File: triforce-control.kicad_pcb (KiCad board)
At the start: 2 copper layers, 107.9 x 64.8 mm, 25 parts, among them U1 ADAFRUIT_HUZZAH, U2 bno055, U3 LPC1768

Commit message: Started new PCB design.
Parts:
- removed CON_D1: Drive Motor 1, mbed:AngledServoCon
- removed CON_D2: Drive Motor 2, mbed:AngledServoCon
- removed CON_D3: Drive Motor 3, mbed:AngledServoCon
- removed CON_RX_D1: Drive Chan 1, mbed:AngledServoCon
- removed CON_RX_D2: Drive Chan 2, mbed:AngledServoCon
- removed CON_RX_D3: Drive Chan 3, mbed:AngledServoCon
- removed CON_RX_D4: Drive Chan 4, mbed:AngledServoCon
- removed CON_RX_D5: Drive Chan 5, mbed:AngledServoCon
- removed CON_RX_D6: Drive Chan 6, mbed:AngledServoCon
- removed CON_RX_W1: Weapon Chan 1, mbed:AngledServoCon
- removed CON_RX_W2: Weapon Chan 2, mbed:AngledServoCon
- removed CON_RX_W3: Weapon Chan 3, mbed:AngledServoCon
- removed CON_RX_W4: Weapon Chan 4, mbed:AngledServoCon
- removed CON_RX_W5: Weapon Chan 5, mbed:AngledServoCon
- removed CON_RX_W6: Weapon Chan 6, mbed:AngledServoCon
- removed CON_W1, CON_W2, CON_W3: Weapon Motor 1, mbed:AngledServoCon
- removed REF** (x4): MountingHole_3.2mm_M3_ISO7380, Mounting_Holes:MountingHole_3.2mm_M3_ISO7380
- added CON1: Conn_01x08, Connectors_JST:JST_PH_S8B-PH-K_08x2.00mm_Angled, B.Cu at (105.4, 69.8)
- added CON2: Conn_01x08, Connectors_JST:JST_PH_S8B-PH-K_08x2.00mm_Angled, B.Cu at (141.6, 69.8)
- added CON3: CON_ESC_W1, mbed:Pin_Header_Angled_3x01_Pitch2.54mm, F.Cu at (135.3, 127.0)
- added CON4: CON_ESC_W2, mbed:Pin_Header_Angled_3x01_Pitch2.54mm, F.Cu at (137.8, 127.0)
- added CON5: CON_ESC_W3, mbed:Pin_Header_Angled_3x01_Pitch2.54mm, F.Cu at (140.3, 127.0)
- added CON6: CON_ESC_D1, mbed:Pin_Header_Angled_3x01_Pitch2.54mm, F.Cu at (142.9, 127.0)
- added CON7: CON_ESC_D2, mbed:Pin_Header_Angled_3x01_Pitch2.54mm, F.Cu at (145.4, 127.0)
- added CON8: CON_ESC_D3, mbed:Pin_Header_Angled_3x01_Pitch2.54mm, F.Cu at (148.0, 127.0)
- added CON9: Conn_01x04, Connectors_JST:JST_PH_S4B-PH-K_04x2.00mm_Angled, F.Cu at (154.7, 126.4)
- added U4: SN65HVD232, Housings_SOIC:SOIC-8_3.9x4.9mm_Pitch1.27mm, B.Cu at (158.1, 139.2)
- moved U3 31.9 mm to (127.0, 94.0), turned to 180 degrees
- moved U1 31.4 mm to (143.5, 86.4)
- moved U2 29.3 mm to (104.1, 137.2), turned to 90 degrees
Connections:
- U3 pad 11: IN_RX_W5 -> IN_RX_W2
- U3 pad 12: IN_RX_W6 -> IN_RX_W1
- U3 pad 19: Net-(U3-Pad19) -> ESP_READY
- U3 pad 21: PWM_OUT_DRV_MOTOR_1 -> PWM_OUT_DRV_MOTOR_3
- U3 pad 23: PWM_OUT_DRV_MOTOR_3 -> PWM_OUT_DRV_MOTOR_1
- U3 pad 24: PWM_OUT_WPN_MOTOR_1 -> PWM_OUT_WPN_MOTOR_3
- U3 pad 26: PWM_OUT_WPN_MOTOR_3 -> PWM_OUT_WPN_MOTOR_1
- U3 pad 29: ESP_READY -> CAN_TXD
- U3 pad 30: Net-(U3-Pad30) -> CAN_RXD
- U3 pad 40: Net-(U3-Pad40) -> MBED_3V3
- U3 pad 5: IN_RX_W1 -> IN_RX_W6
- U3 pad 6: IN_RX_W2 -> IN_RX_W5
- U3 pad 7: IN_RX_W3 -> IN_RX_W4
- U3 pad 8: IN_RX_W4 -> IN_RX_W3
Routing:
- net CAN_TXD: track 0.00 -> 93.9 mm
- net CAN_RXD: track 0.00 -> 85.1 mm
- net MBED_3V3: track 0.00 -> 62.0 mm, vias 0 -> 1
- net IN_RX_W4: track 19.2 -> 72.6 mm
- net IN_RX_W3: track 15.6 -> 68.5 mm
- net IN_RX_W6: track 30.8 -> 80.6 mm
- net IN_RX_W5: track 27.2 -> 76.6 mm
- net IN_RX_W2: track 12.0 -> 59.4 mm
- net IN_RX_W1: track 8.45 -> 55.7 mm
- net +5V: track 194.6 -> 231.5 mm
- net BNO_MBED_SCL: track 56.4 -> 22.4 mm
- net GND: track 213.0 -> 188.2 mm, vias 0 -> 4
- net IN_RX_D6: track 53.9 -> 33.8 mm
- net IN_RX_D1: track 35.9 -> 50.7 mm
- net IN_RX_D5: track 50.3 -> 37.2 mm
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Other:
- board size 107.9 x 64.8 mm -> 74 x 86 mm
- board text added: "Triforce Fight Controller V1"
- board text removed: "DRIVE_RX"
- board text removed: "ESC OUT"
- board text removed: "WEAPON_RX"

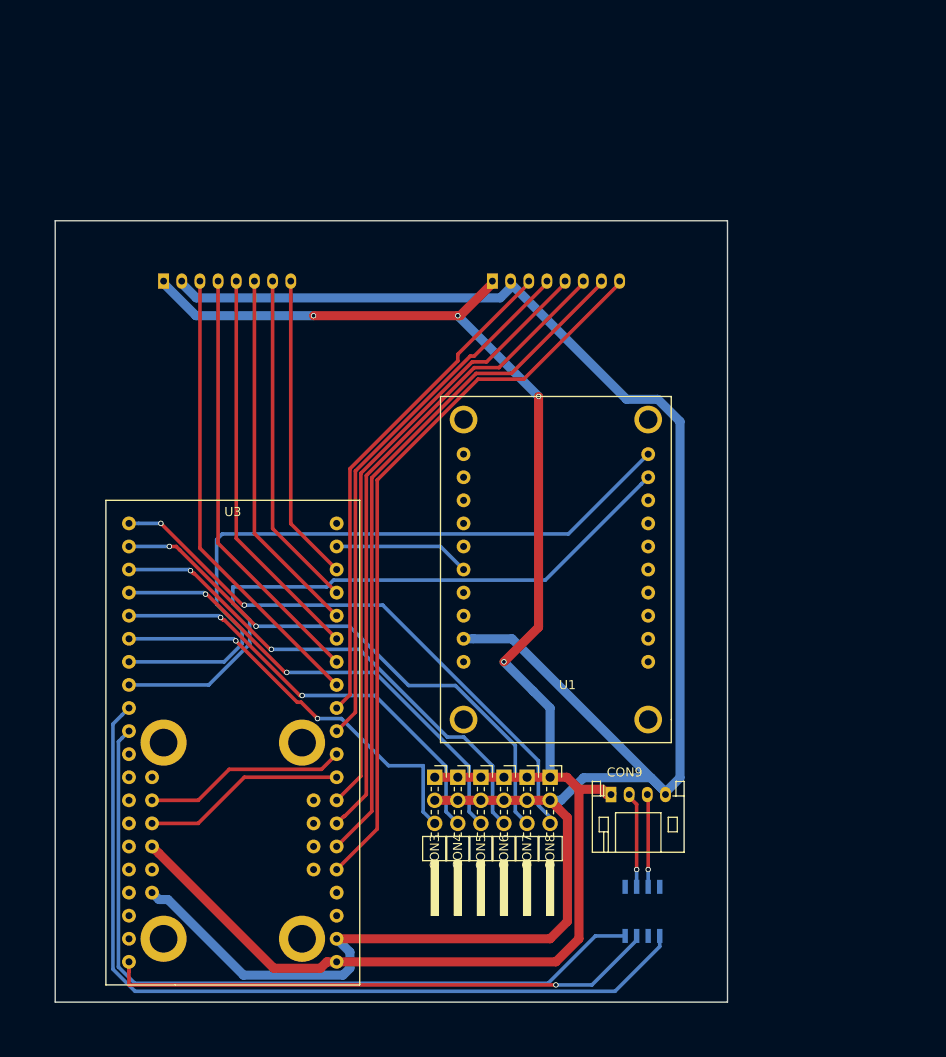
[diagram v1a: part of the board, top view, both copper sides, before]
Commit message: Added missing GND connection.
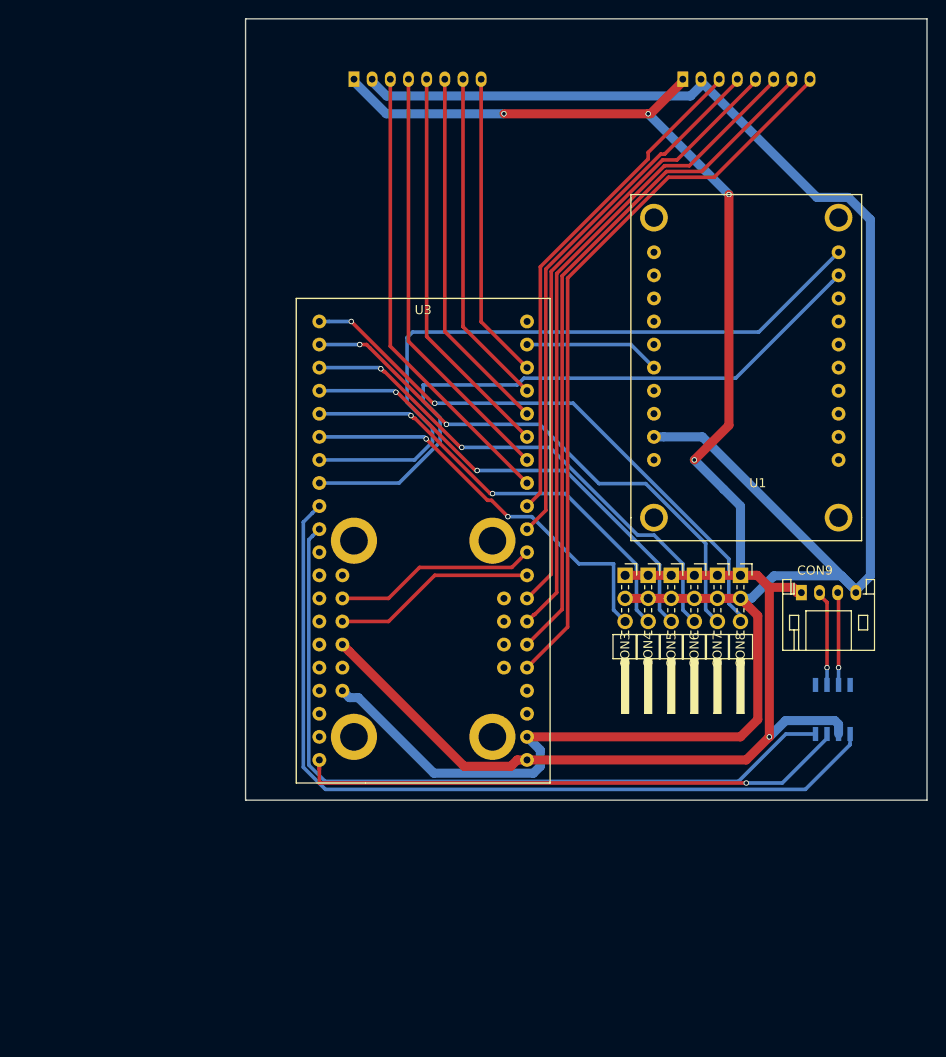
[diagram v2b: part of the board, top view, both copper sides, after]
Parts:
- moved U3 30.5 mm to (148.0, 71.8)
- moved CON2 30.5 mm to (162.6, 47.6)
- moved CON3 30.5 mm to (156.2, 104.8)
- moved CON4 30.5 mm to (158.8, 104.8)
- moved CON6 30.5 mm to (163.8, 104.8)
- moved CON7 30.5 mm to (166.4, 104.8)
- moved CON9 30.5 mm to (175.6, 104.1)
- moved U1 30.5 mm to (164.5, 64.1)
- moved CON1 30.5 mm to (126.4, 47.6)
- moved U2 30.5 mm to (125.1, 114.9)
- moved CON5 30.5 mm to (161.3, 104.8)
- moved CON8 30.5 mm to (168.9, 104.8)
- moved U4 30.5 mm to (179.1, 117.0)
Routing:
- net GND: track 188.2 -> 197.8 mm, vias 4 -> 5
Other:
- board size 74 x 86 mm -> 75 x 86 mm

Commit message: Prettifying the front silkscreen with symbols and text.
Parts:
- added G***: LOGO, mbed:logo_small, F.Cu at (134.0, 54.6)
- added REF***: OSHW-Logo2_14.6x12mm_SilkScreen, Symbols:OSHW-Logo2_14.6x12mm_SilkScreen, F.Cu at (134.0, 80.6)
- added REF***: KiCad-Logo2_6mm_SilkScreen, Symbols:KiCad-Logo2_6mm_SilkScreen, F.Cu at (151.8, 45.1)
- added REF1: MountingHole_3.2mm_M3_ISO14580_Pad, Mounting_Holes:MountingHole_3.2mm_M3_ISO14580_Pad, F.Cu at (120.0, 56.0)
- added REF2: MountingHole_3.2mm_M3_ISO14580_Pad, Mounting_Holes:MountingHole_3.2mm_M3_ISO14580_Pad, F.Cu at (184.0, 56.0)
- added REF3: MountingHole_3.2mm_M3_ISO14580_Pad, Mounting_Holes:MountingHole_3.2mm_M3_ISO14580_Pad, F.Cu at (152.0, 114.0)
- added U3: LPC1768, mbed:lpc1768, F.Cu at (148.0, 71.8)
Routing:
- net (no net): track 2.54 -> 0.00 mm
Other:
- board text added: "CAN BUS"
- board text added: "DRIVE RX"
- board text added: "DRV"
- board text added: "ESC PWM OUT"
- board text added: "TeamTriforceUK"
- board text added: "WEAPON RX"
- board text added: "WPN"
- board text added: "fb.com/TeamTriforceUK"
- board text added: "github.com/TeamTriforceUK"
- board text removed: "Triforce Fight Controller"

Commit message: Changed tracks.
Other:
- board text added: "Triforce Fight Controller v1.0 (keffel)"
- board text removed: "Rev. A"
- board text removed: "Triforce Fight Controller V1"

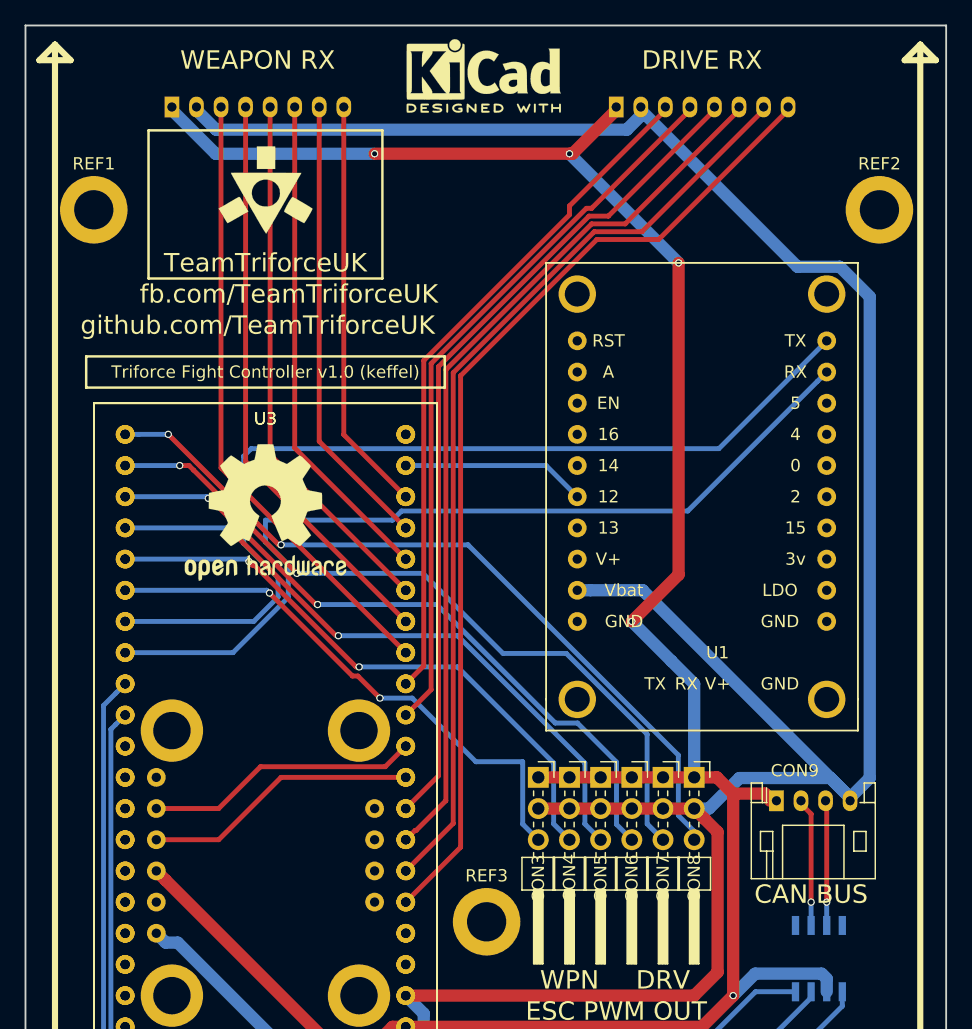
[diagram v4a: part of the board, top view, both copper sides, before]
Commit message: Swapped JSP PH for JST SH on RX inputs.
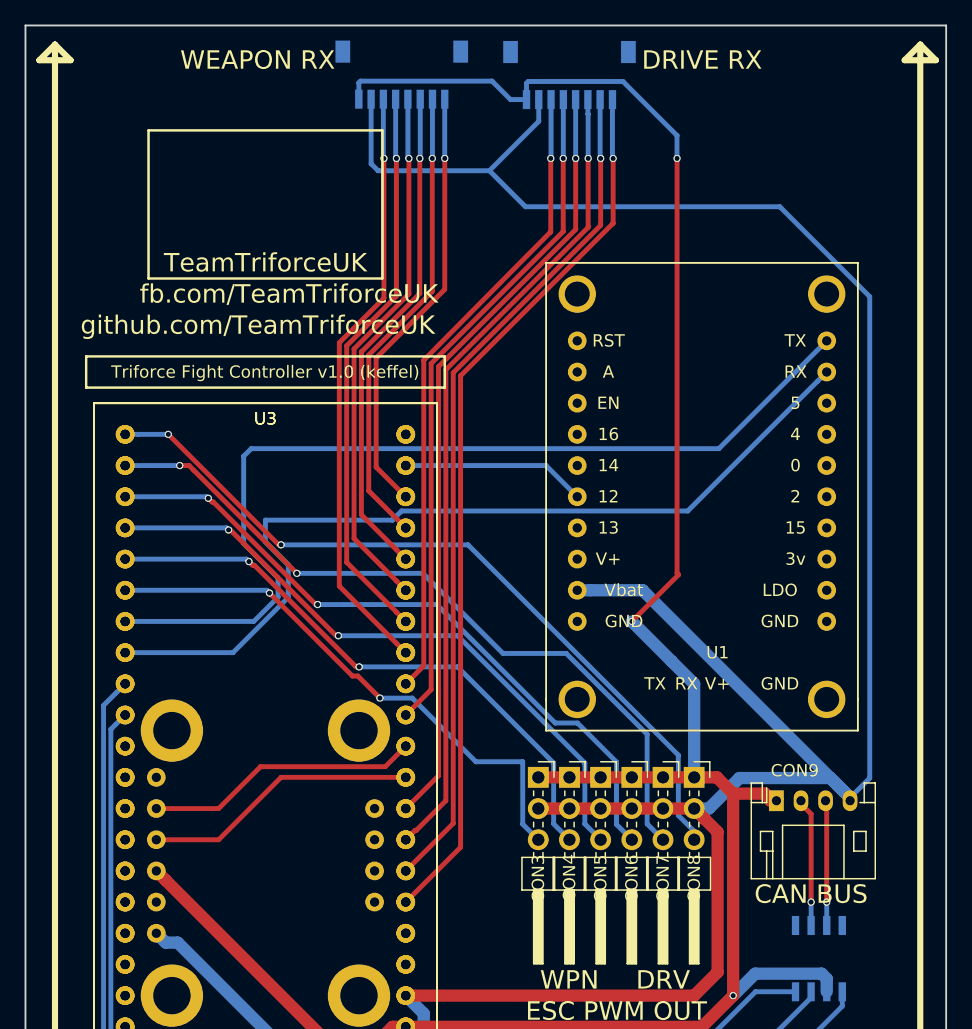
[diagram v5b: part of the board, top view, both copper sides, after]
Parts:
- removed G***: LOGO, mbed:logo_small
- removed REF***: OSHW-Logo2_14.6x12mm_SilkScreen, Symbols:OSHW-Logo2_14.6x12mm_SilkScreen
- removed REF***: KiCad-Logo2_6mm_SilkScreen, Symbols:KiCad-Logo2_6mm_SilkScreen
- removed REF1, REF2, REF3: MountingHole_3.2mm_M3_ISO14580_Pad, Mounting_Holes:MountingHole_3.2mm_M3_ISO14580_Pad
- CON1, CON2: footprint Connectors_JST:JST_PH_S8B-PH-K_08x2.00mm_Angled -> Connectors_JST:JST_SH_SM08B-SRSS-TB_08x1.00mm_Angled
- moved CON1 18.9 mm to (145.1, 45.1)
- moved CON2 4.58 mm to (158.8, 45.1)
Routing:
- net GND: track 197.8 -> 187.1 mm, vias 5 -> 3
- net IN_RX_W6: track 80.6 -> 72.5 mm, vias 0 -> 1
- net IN_RX_W5: track 76.6 -> 69.4 mm, vias 0 -> 1
- net IN_RX_W4: track 72.6 -> 66.5 mm, vias 0 -> 1
- net +5V: track 231.5 -> 225.9 mm
- net IN_RX_W3: track 68.5 -> 63.5 mm, vias 0 -> 1
- net IN_RX_W2: track 59.4 -> 55.4 mm, vias 0 -> 1
- net IN_RX_W1: track 55.7 -> 52.5 mm, vias 0 -> 1
- net IN_RX_D6: track 33.8 -> 35.7 mm, vias 0 -> 1
- net IN_RX_D1: track 50.7 -> 48.9 mm, vias 0 -> 1
- net IN_RX_D5: track 37.2 -> 38.3 mm, vias 0 -> 1
- net IN_RX_D2: track 47.3 -> 46.2 mm, vias 0 -> 1
- net IN_RX_D4: track 40.6 -> 40.9 mm, vias 0 -> 1
- net IN_RX_D3: track 43.9 -> 43.6 mm, vias 0 -> 1
